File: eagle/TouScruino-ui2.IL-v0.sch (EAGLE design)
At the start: 3 parts, among them U1 TFT_20

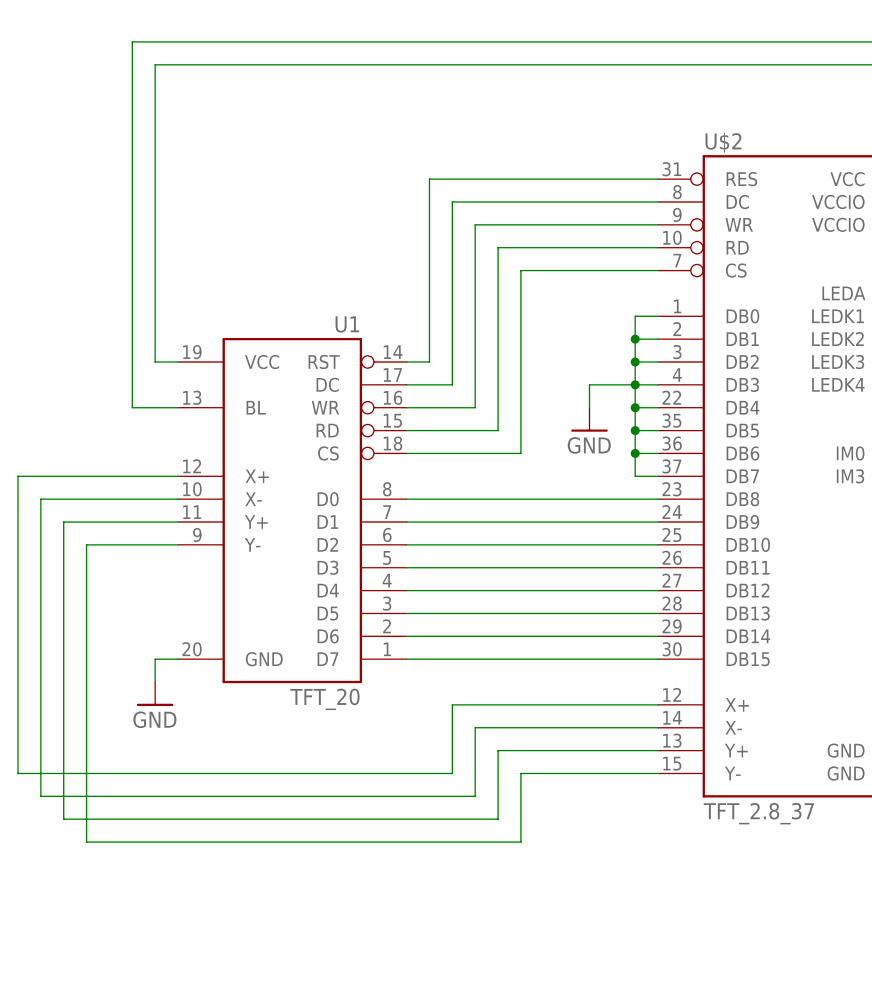
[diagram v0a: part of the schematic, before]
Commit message: 
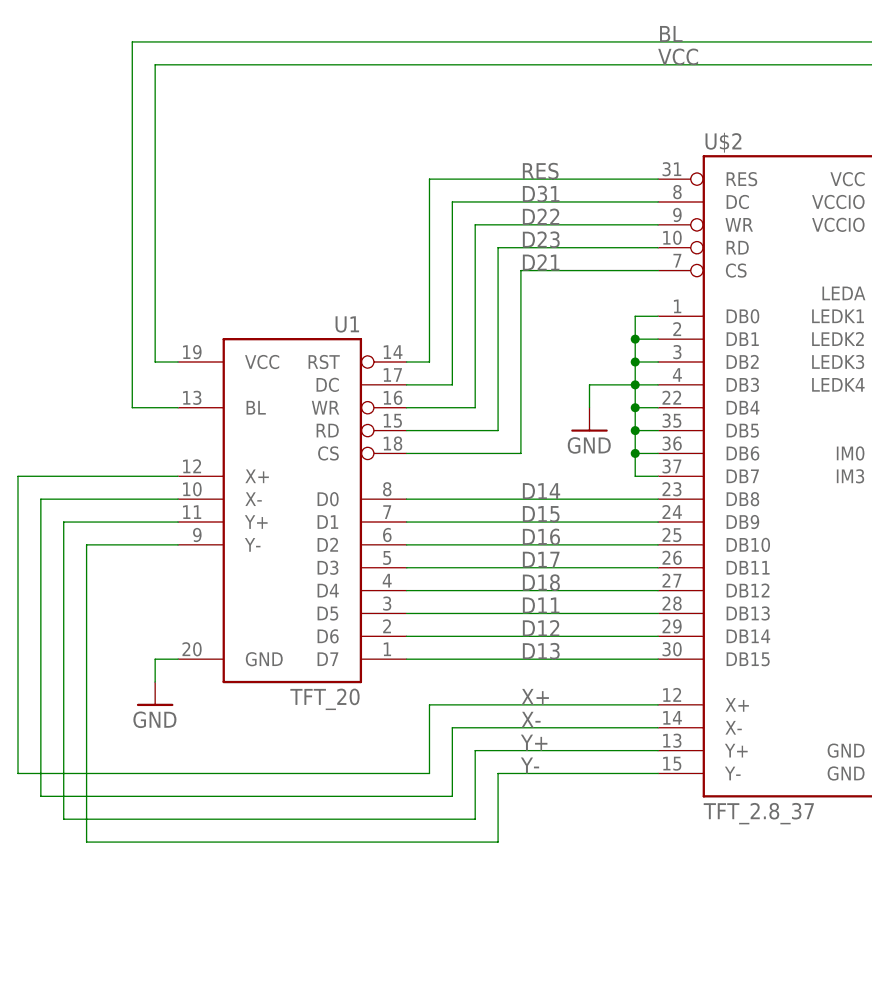
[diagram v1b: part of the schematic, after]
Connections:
- net N$1 renamed VCC
- net N$10 renamed D31
- net N$11 renamed D22
- net N$12 renamed D23
- net N$13 renamed D21
- net N$14 renamed D16
- net N$15 renamed D17
- net N$16 renamed D18
- net N$17 renamed D11
- net N$18 renamed D12
- net N$19 renamed D13
- net N$2 renamed BL
- net N$3 renamed D14
- net N$4 renamed D15
- net N$5 renamed Y-
- net N$6 renamed Y+
- net N$7 renamed X-
- net N$8 renamed X+
- net N$9 renamed RES

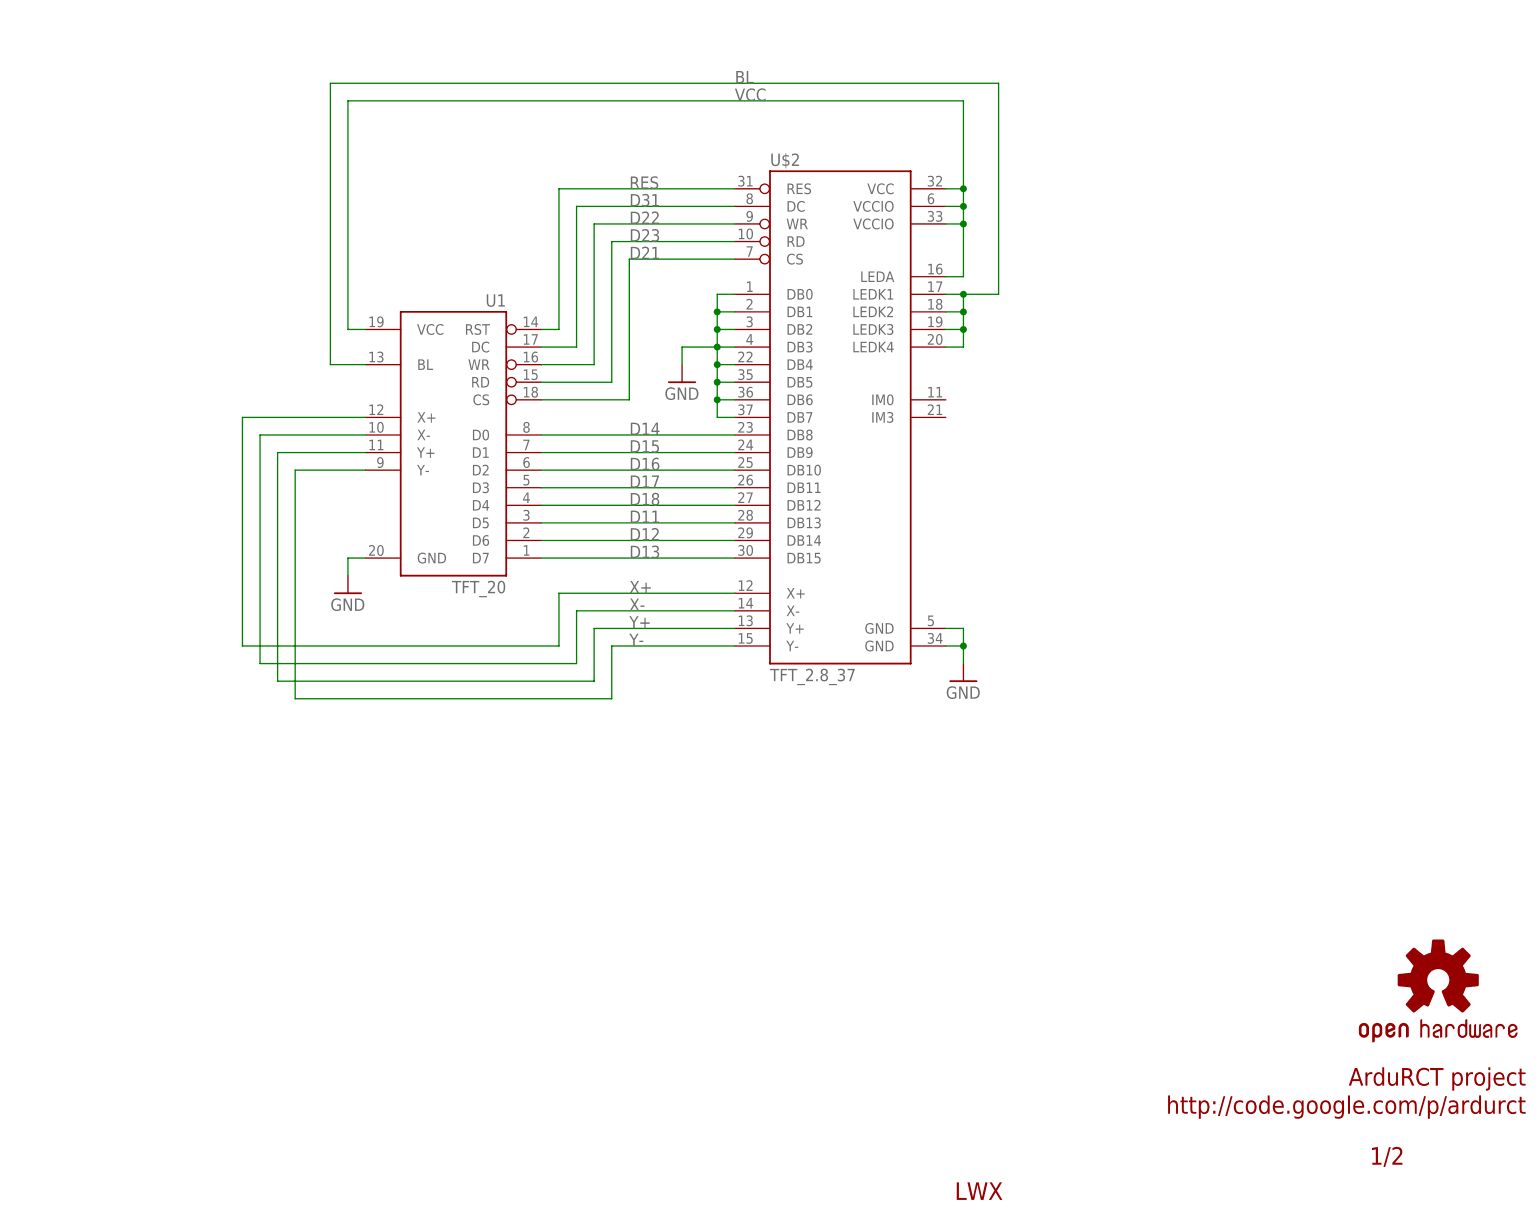
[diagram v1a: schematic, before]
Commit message: 
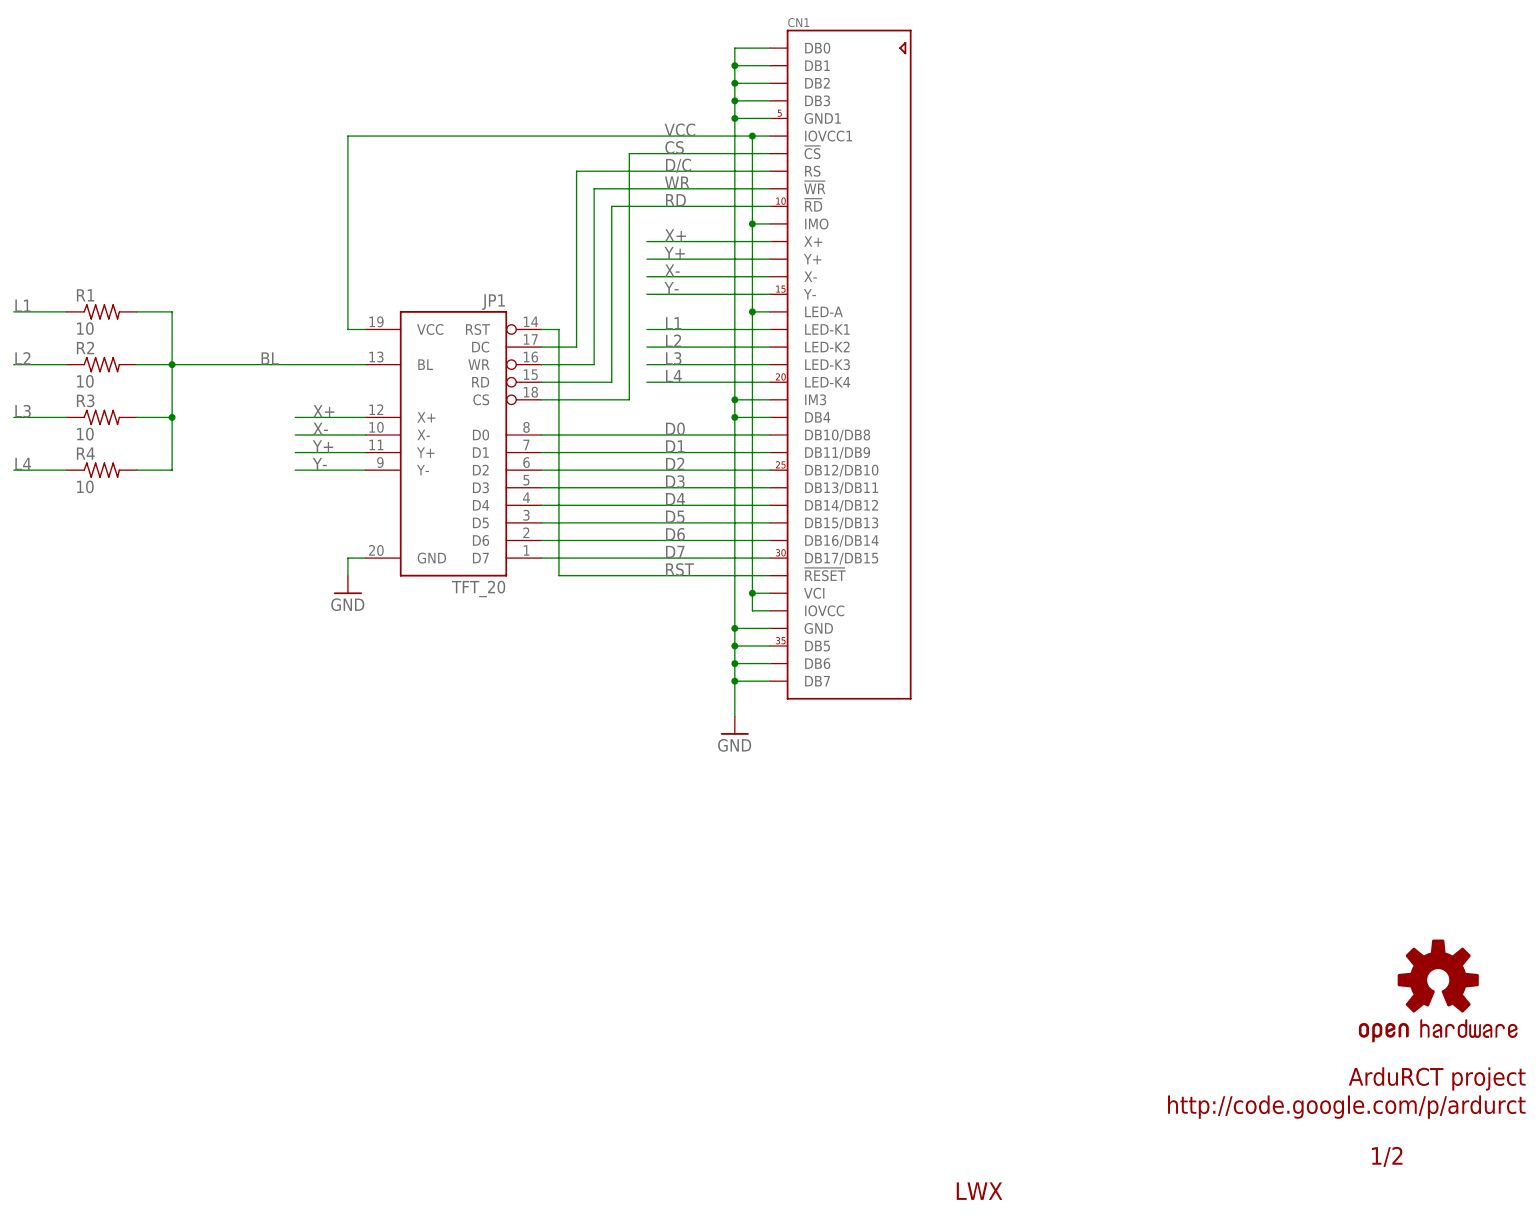
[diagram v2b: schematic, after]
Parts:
- removed U$2: TFT_2.8_37, wibauxl:TFT_2.8_37
- added CN1: (no value), adafruit:ILI9325_LCD1.0MM
- added R1, R2, R3, R4: 10, resistor:R-US_R0603
- renumbered U1 to JP1
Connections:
- removed net D11: JP1.D5, U$2.DB13
- removed net D12: JP1.D6, U$2.DB14
- removed net D13: JP1.D7, U$2.DB15
- removed net D14: JP1.D0, U$2.DB8
- removed net D15: JP1.D1, U$2.DB9
- removed net D16: JP1.D2, U$2.DB10
- removed net D17: JP1.D3, U$2.DB11
- removed net D18: JP1.D4, U$2.DB12
- removed net D21: JP1.CS, U$2.CS
- removed net D22: JP1.WR, U$2.WR
- removed net D23: JP1.RD, U$2.RD
- removed net D31: JP1.DC, U$2.DC
- removed net RES: JP1.RST, U$2.RES
- new net CS: CN1.!CS, JP1.CS
- new net D/C: CN1.RS, JP1.DC
- new net D0: CN1.DB10/DB8, JP1.D0
- new net D1: CN1.DB11/DB9, JP1.D1
- new net D2: CN1.DB12/DB10, JP1.D2
- new net D3: CN1.DB13/DB11, JP1.D3
- new net D4: CN1.DB14/DB12, JP1.D4
- new net D5: CN1.DB15/DB13, JP1.D5
- new net D6: CN1.DB16/DB14, JP1.D6
- new net D7: CN1.DB17/DB15, JP1.D7
- new net L1: CN1.LED-K1, R1.1
- new net L2: CN1.LED-K2, R2.1
- new net L3: CN1.LED-K3, R3.1
- new net L4: CN1.LED-K4, R4.1
- new net RD: CN1.!RD, JP1.RD
- new net RST: CN1.!RESET, JP1.RST
- new net WR: CN1.!WR, JP1.WR
- net BL: now also R1.2, R2.2, R3.2, R4.2; no longer U$2.LEDK1, U$2.LEDK2, U$2.LEDK3, U$2.LEDK4
- net GND: now also CN1.DB0, CN1.DB1, CN1.DB2, CN1.DB3, CN1.DB4, CN1.DB5, CN1.DB6, CN1.DB7, CN1.GND, CN1.GND1, CN1.IM3; no longer U$2.DB0, U$2.DB1, U$2.DB2, U$2.DB3, U$2.DB4, U$2.DB5, U$2.DB6, U$2.DB7, U$2.GND@1, U$2.GND@2
- net VCC: now also CN1.IMO, CN1.IOVCC, CN1.IOVCC1, CN1.LED-A, CN1.VCI; no longer U$2.LEDA, U$2.VCC, U$2.VCCIO@1, U$2.VCCIO@2
- net X+: now also CN1.X+; no longer U$2.X+
- net X-: now also CN1.X-; no longer U$2.X-
- net Y+: now also CN1.Y+; no longer U$2.Y+
- net Y-: now also CN1.Y-; no longer U$2.Y-
